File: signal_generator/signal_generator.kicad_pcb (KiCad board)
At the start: 2 copper layers, 100 x 100 mm, 21 parts, among them J1 DAC_OUT, U1 Digilent_CMOD-S7_25, U2 ADC9765, U3 TL072

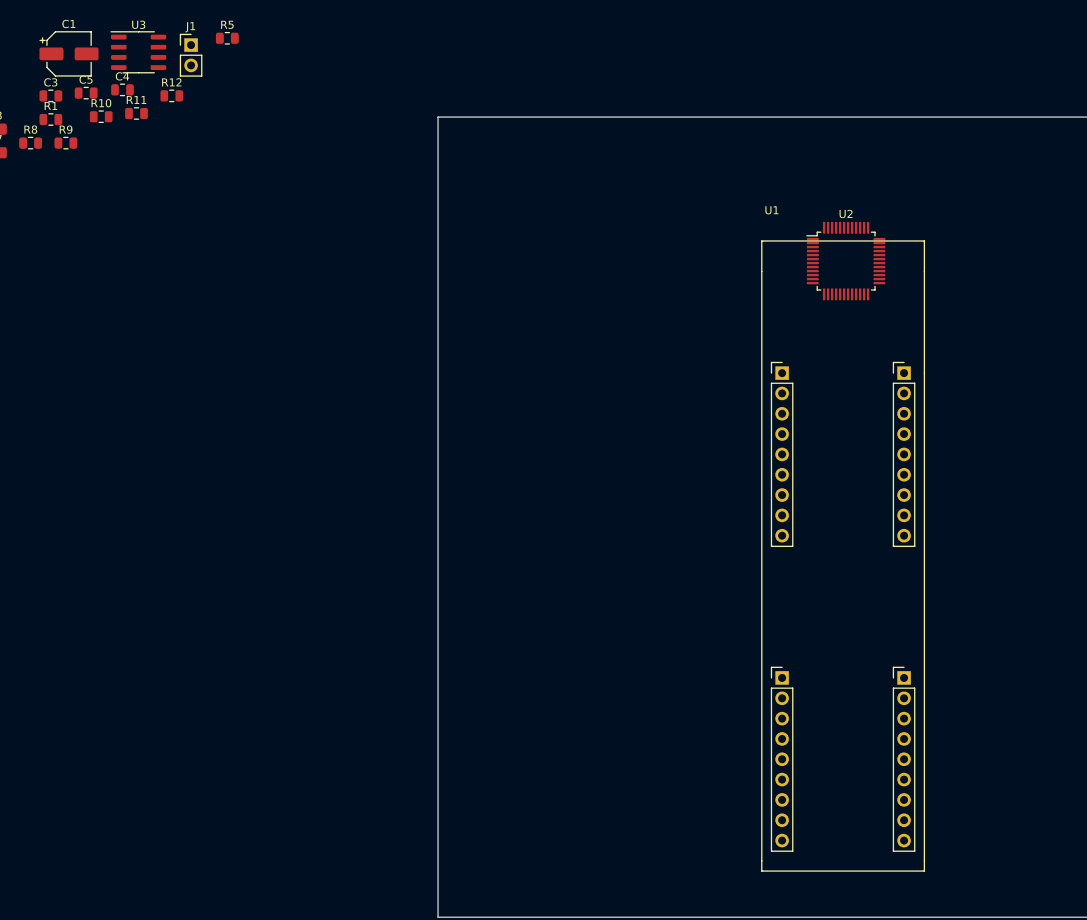
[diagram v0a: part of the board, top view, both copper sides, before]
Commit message: new pcb design and pin layout
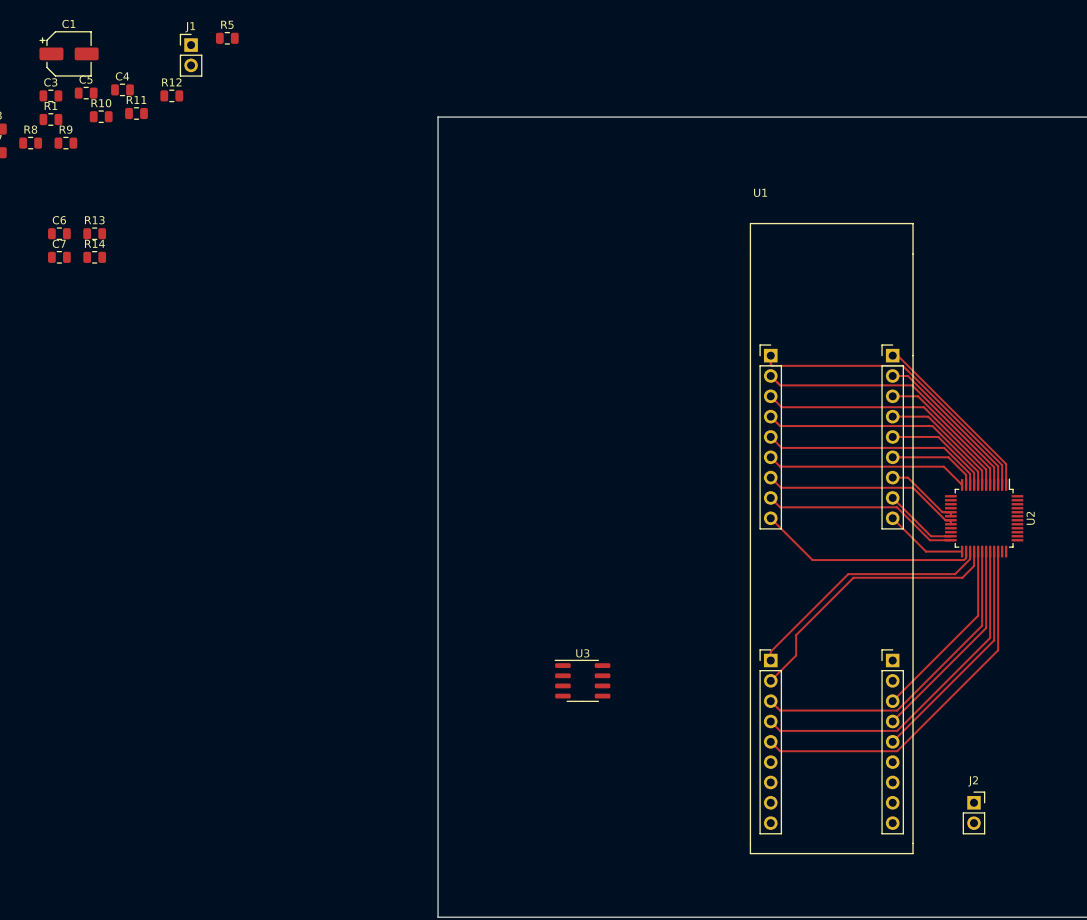
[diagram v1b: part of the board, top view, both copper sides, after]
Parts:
- added C6: 22nF, Capacitor_SMD:C_0805_2012Metric, F.Cu at (106.7, 68.6)
- added C7: 22nF, Capacitor_SMD:C_0805_2012Metric, F.Cu at (106.7, 71.5)
- added J2: USB/Ext., Connector_PinSocket_2.54mm:PinSocket_1x02_P2.54mm_Vertical, F.Cu at (221.0, 139.7)
- added R13: 256, Resistor_SMD:R_0805_2012Metric, F.Cu at (111.1, 68.6)
- added R14: 256, Resistor_SMD:R_0805_2012Metric, F.Cu at (111.1, 71.5)
- moved U3 96.2 mm to (172.1, 124.5)
- moved U2 36.5 mm to (222.2, 104.1), turned to 270 degrees
- moved U1 2.60 mm to (195.6, 83.8)
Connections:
- U1 pad 1: /DB0P1 -> /DB10P1
- U1 pad 16: /DB9P1 -> /DB7P2
- U1 pad 17: /DB10P1 -> /DB6P2
- U1 pad 18: /DB11P1 -> /DB4P2
- U1 pad 19: /DB0P2 -> /DB2P2
- U1 pad 2: /DB1P1 -> /DB8P1
- U1 pad 20: /DB1P2 -> /DB0P2
- U1 pad 21: /BD2P2 -> Net-(U1-Pad21)
- U1 pad 22: /BD3P2 -> Net-(U1-Pad22)
- U1 pad 23: /BD4P2 -> Net-(U1-Pad23)
- U1 pad 24: +5VD -> Net-(J2-Pad2)
- U1 pad 29: Net-(U1-Pad29) -> /DB1P2
- U1 pad 3: /DB2P1 -> /DB6P1
- U1 pad 30: Net-(U1-Pad30) -> /DB3P2
- U1 pad 31: Net-(U1-Pad31) -> /DB5P2
- U1 pad 4: /DB3P1 -> /DB4P1
- U1 pad 40: /SLEEP -> /DB9P2
- U1 pad 41: /CLK_1MHz -> /DB11P2
- U1 pad 42: /BD11P2 -> /CLK_1MHz
- U1 pad 43: /BD10P2 -> /DB1P1
- U1 pad 44: /BD9P2 -> /DB3P1
- U1 pad 45: /BD8P2 -> /DB5P1
- U1 pad 46: /BD7P2 -> /DB7P1
- U1 pad 47: /BD6P2 -> /DB9P1
- U1 pad 48: /BD5P2 -> /DB11P1
- U1 pad 5: /DB4P1 -> /DB2P1
- U1 pad 6: /DB5P1 -> /DB0P1
- U1 pad 7: /DB6P1 -> /CLK_1MHz
- U1 pad 8: /DB7P1 -> /DB10P2
- U1 pad 9: /DB8P1 -> /DB8P2
- U2 pad 16: +5VD -> +3V3
- U2 pad 22: +5VD -> +3V3
- U2 pad 23: /BD11P2 -> /DB11P2
- U2 pad 24: /BD10P2 -> /DB10P2
- U2 pad 25: /BD9P2 -> /DB9P2
- U2 pad 26: /BD8P2 -> /DB8P2
- U2 pad 27: /BD7P2 -> /DB7P2
- U2 pad 28: /BD6P2 -> /DB6P2
- U2 pad 29: /BD5P2 -> /DB5P2
- U2 pad 30: /BD4P2 -> /DB4P2
- U2 pad 31: /BD3P2 -> /DB3P2
- U2 pad 32: /BD2P2 -> /DB2P2
- U2 pad 47: +5VA -> +3.3VA
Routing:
- net /DB0P2: track 0.00 -> 46.5 mm
- net /DB2P2: track 0.00 -> 43.5 mm
- net /DB4P2: track 0.00 -> 40.6 mm
- net /DB10P1: track 0.00 -> 37.7 mm
- net /DB8P1: track 0.00 -> 34.9 mm
- net /CLK_1MHz: track 0.00 -> 34.8 mm
- net /DB6P2: track 0.00 -> 34.7 mm
- net /DB6P1: track 0.00 -> 32.6 mm
- net /DB7P2: track 0.00 -> 31.8 mm
- net /DB4P1: track 0.00 -> 30.4 mm
- net /DB1P2: track 0.00 -> 29.0 mm
- net /DB2P1: track 0.00 -> 28.2 mm
- net /DB8P2: track 0.00 -> 27.5 mm
- net /DB3P2: track 0.00 -> 26.1 mm
- net /DB0P1: track 0.00 -> 25.4 mm
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
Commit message: added power supply, integrated in schematic
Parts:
- removed C4, C5: C_Small, Capacitor_SMD:C_0805_2012Metric
- removed C6, C7: 22nF, Capacitor_SMD:C_0805_2012Metric
- removed J2: USB/Ext., Connector_PinSocket_2.54mm:PinSocket_1x02_P2.54mm_Vertical
- removed R1, R2: 2k, Resistor_SMD:R_0805_2012Metric
- removed R13, R14: 256, Resistor_SMD:R_0805_2012Metric
- removed R3, R4, R5, R6: 25R, Resistor_SMD:R_0805_2012Metric
- removed R9: 225R, Resistor_SMD:R_0805_2012Metric
- removed U1: Digilent_CMOD-S7_25, signal_generator:CMODS7-25
- removed U2: ADC9765, Package_QFP:LQFP-48_7x7mm_P0.5mm
- removed U3: TL072, Package_SO:SOIC-8_3.9x4.9mm_P1.27mm
- added C101: 22nF, Capacitor_SMD:C_0603_1608Metric, F.Cu at (238.5, 100.6)
- added C102: 22nF, Capacitor_SMD:C_0603_1608Metric, F.Cu at (238.5, 90.3)
- added C201: 10u, DSC-Supply:153CLV-0405, F.Cu at (217.4, 129.0)
- added C202: 22u, DSC-Supply:C0805, F.Cu at (231.6, 120.9)
- added C203: 100nF, Capacitor_SMD:C_0603_1608Metric, F.Cu at (232.9, 89.7)
- added C204: 100nF, Capacitor_SMD:C_0603_1608Metric, F.Cu at (249.4, 108.0)
- added C205: 100nF, Capacitor_SMD:C_0603_1608Metric, F.Cu at (219.7, 93.7)
- added C206: 10u, DSC-Supply:153CLV-0405, F.Cu at (221.5, 122.9)
- added C207: 100nF, Capacitor_SMD:C_0603_1608Metric, F.Cu at (219.7, 96.8)
- added C208: 100nF, Capacitor_SMD:C_0603_1608Metric, F.Cu at (237.5, 108.0)
- added C209: 2u2, DSC-Supply:C0805, F.Cu at (227.1, 126.0)
- added C210: 1n, DSC-Supply:C0805, F.Cu at (231.6, 132.1)
- added C211: 22u, DSC-Supply:C0805, F.Cu at (227.1, 132.1)
- added C212: 10u, DSC-Supply:153CLV-0405, F.Cu at (236.7, 127.0)
- added C213: 10u, DSC-Supply:153CLV-0405, F.Cu at (244.9, 127.5)
- added D201: MBR0520LT, DSC-Supply:SOD123, F.Cu at (226.6, 134.6)
- added J101: DAC_OUT_BUF, Connector_PinHeader_2.54mm:PinHeader_1x02_P2.54mm_Vertical, F.Cu at (328.2, 66.9)
- added J201: Power Input, Connector_PinSocket_2.54mm:PinSocket_1x02_P2.54mm_Vertical, F.Cu at (216.9, 134.6)
- added J202: Power Output, Connector_PinHeader_2.54mm:PinHeader_1x05_P2.54mm_Vertical, F.Cu at (230.6, 117.1)
- added L201: 22u, DSC-Supply:L0315, F.Cu at (227.1, 122.9)
- added L202: 22u, DSC-Supply:L0315, F.Cu at (227.1, 129.0)
- added L203: 5uH, Inductor_SMD:L_0805_2012Metric, F.Cu at (234.2, 113.3)
- added R101: 256, Resistor_SMD:R_0603_1608Metric, F.Cu at (238.5, 98.7)
- added R102: 256, Resistor_SMD:R_0603_1608Metric, F.Cu at (238.5, 92.2)
- added R103: 2k, Resistor_SMD:R_0603_1608Metric, F.Cu at (238.5, 96.8)
- added R104: 2k, Resistor_SMD:R_0603_1608Metric, F.Cu at (238.5, 94.1)
- added R105: 25R, Resistor_SMD:R_0603_1608Metric, F.Cu at (234.9, 94.2)
- added R106: 25R, Resistor_SMD:R_0603_1608Metric, F.Cu at (234.9, 97.0)
- added R107: 25R, Resistor_SMD:R_0603_1608Metric, F.Cu at (234.9, 92.2)
- added R108: 25R, Resistor_SMD:R_0603_1608Metric, F.Cu at (234.9, 99.1)
- added R111: 225R, Resistor_SMD:R_0603_1608Metric, F.Cu at (328.2, 115.3)
- added R113: R_Small, Resistor_SMD:R_0603_1608Metric, F.Cu at (337.1, 69.0)
- added R114: R_Small, Resistor_SMD:R_0603_1608Metric, F.Cu at (332.7, 71.9)
- added R117: R_Small, Resistor_SMD:R_0603_1608Metric, F.Cu at (328.1, 74.9)
- added R118: R_Small, Resistor_SMD:R_0603_1608Metric, F.Cu at (332.5, 74.9)
- added R201: 29k4, DSC-Supply:C0805, F.Cu at (231.6, 129.5)
- added R202: 10k, DSC-Supply:C0805, F.Cu at (231.6, 134.6)
- added R203: 30k, DSC-Supply:C0805, F.Cu at (240.8, 123.4)
- added R204: 30k, DSC-Supply:C0805, F.Cu at (240.8, 120.9)
- added R205: 30k, DSC-Supply:C0805, F.Cu at (249.4, 123.4)
- added R206: 30k, DSC-Supply:C0805, F.Cu at (249.4, 120.9)
- added RV101: 10kB, Potentiometer_THT:Potentiometer_Alpha_RD901F-40-00D_Single_Vertical_CircularHoles, F.Cu at (225.1, 59.4)
- added RV102: 10kB, Potentiometer_THT:Potentiometer_Alpha_RD901F-40-00D_Single_Vertical_CircularHoles, F.Cu at (225.1, 73.7)
- added RV103: 10kB, Potentiometer_THT:Potentiometer_Alpha_RD901F-40-00D_Single_Vertical_CircularHoles, F.Cu at (239.9, 59.4)
- added RV104: 10kB, Potentiometer_THT:Potentiometer_Alpha_RD901F-40-00D_Single_Vertical_CircularHoles, F.Cu at (239.9, 73.7)
- added U101: Digilent_CMOD-S7_25, signal_generator:CMODS7-25, F.Cu at (195.1, 72.6)
- added U102: ADC9765, Package_QFP:LQFP-48_7x7mm_P0.5mm, F.Cu at (227.1, 95.0)
- added U103: TL074, Package_SO:SSOP-14_5.3x6.2mm_P0.65mm, F.Cu at (243.6, 108.7)
- added U201: TPS76933, DSC-Supply:SOT23-DBV, F.Cu at (222.0, 127.5)
- added U202: LM2611, DSC-Supply:SOT23-DBV, F.Cu at (231.6, 126.0)
- added U203: TPS76901, DSC-Supply:SOT23-DBV, F.Cu at (240.8, 127.5)
- added U204: TPS72301, DSC-Supply:SOT23-DBV, F.Cu at (249.4, 127.5)
- C103: renamed from C1; footprint Capacitor_SMD:CP_Elec_5x5.3 -> DSC-Supply:153CLV-0405
- C104: renamed from C2; footprint Capacitor_SMD:C_0805_2012Metric -> Capacitor_SMD:C_0603_1608Metric
- C105: renamed from C3; footprint Capacitor_SMD:C_0805_2012Metric -> Capacitor_SMD:C_0603_1608Metric
- R109: renamed from R7; footprint Resistor_SMD:R_0805_2012Metric -> Resistor_SMD:R_0603_1608Metric
- R110: renamed from R8; footprint Resistor_SMD:R_0805_2012Metric -> Resistor_SMD:R_0603_1608Metric
- R112: renamed from R10; footprint Resistor_SMD:R_0805_2012Metric -> Resistor_SMD:R_0603_1608Metric
- R115: renamed from R11; footprint Resistor_SMD:R_0805_2012Metric -> Resistor_SMD:R_0603_1608Metric
- R116: renamed from R12; footprint Resistor_SMD:R_0805_2012Metric -> Resistor_SMD:R_0603_1608Metric
- moved C104 253.5 mm to (324.6, 112.3), turned to 270 degrees
- moved R115 220.4 mm to (329.7, 108.7), turned to 180 degrees
- moved R110 185.1 mm to (278.3, 116.9)
- moved R112 185.1 mm to (287.2, 113.6)
- moved C105 185.1 mm to (280.9, 111.0)
- moved J102 185.1 mm to (298.4, 104.7)
- moved R109 185.1 mm to (273.9, 118.1)
- moved R116 185.1 mm to (296.0, 111.0)
- moved C103 144.0 mm to (242.8, 96.5), turned to 90 degrees
- renumbered J1 to J102
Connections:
- net Net-(C2-Pad1) renamed /I_OUT1-
- net Net-(C2-Pad2) renamed /I_OUT1+
- net Net-(C3-Pad1) renamed /I_OUT2-
- C105 pad 2: Net-(C3-Pad2) -> /I_OUT2+
- J102 pad 2: /DAC_OUT1 -> /DAC_OUT2
- R116 pad 1: /DAC_OUT1 -> /DAC_OUT2
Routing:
- net +3V3: track 0.00 -> 60.0 mm, vias 0 -> 1
- net VDDA: track 0.00 -> 47.5 mm, vias 0 -> 1
- net -5V: track 0.00 -> 38.1 mm
- net /CLK_1MHz: track 34.8 -> 0.00 mm
- net /SLEEP: track 0.00 -> 34.5 mm
- net /CLK_2: track 0.00 -> 31.4 mm
- net +5V: track 0.00 -> 23.5 mm, vias 0 -> 3
- net VSSA: track 0.00 -> 18.3 mm
- net /CLK_1: track 0.00 -> 15.9 mm
- net /I_OUT1-: track 0.00 -> 13.7 mm
- net Net-(C209-Pad2): track 0.00 -> 12.3 mm
- net Net-(C103-Pad1): track 0.00 -> 12.2 mm
- net /I_OUT1+: track 0.00 -> 12.0 mm
- net Net-(C209-Pad1): track 0.00 -> 9.84 mm
- net Net-(R102-Pad1): track 0.00 -> 9.75 mm
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- added copper zone on B.Cu, net +5V
- added copper zone on F.Cu, net GND
- added copper zone on F.Cu, net GNDA
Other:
- board size 100 x 100 mm -> 100 x 85 mm

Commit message: finished PCB v1
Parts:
- added G***: LOGO, resona_logo:Logo_kicad_teeny, F.Cu at (220.0, 68.3)
- C101, C102, C104, C105, C203, C204, C205, C207, C208: footprint Capacitor_SMD:C_0603_1608Metric -> Capacitor_SMD:C_0603_1608Metric_Pad1.08x0.95mm_HandSolder
- C103: footprint DSC-Supply:153CLV-0405 -> Capacitor_SMD:C_0603_1608Metric_Pad1.08x0.95mm_HandSolder
- L203: footprint Inductor_SMD:L_0805_2012Metric -> Inductor_THT:L_Axial_L7.0mm_D3.3mm_P10.16mm_Horizontal_Fastron_MICC
- R101, R102, R103, R104, R105, R106, R107, R108, R109, R110, R111, R112, R113, R114, R115, R116, R117, R118: footprint Resistor_SMD:R_0603_1608Metric -> Resistor_SMD:R_0603_1608Metric_Pad0.98x0.95mm_HandSolder
- RV103, RV104: value 10kB -> 10kA
- U103: footprint Package_SO:SSOP-14_5.3x6.2mm_P0.65mm -> Package_SO:SOIC-14_3.9x8.7mm_P1.27mm
- moved R113 90.2 mm to (254.5, 105.2), turned to 270 degrees
- moved R111 86.5 mm to (242.3, 104.9)
- moved R115 86.0 mm to (244.2, 99.2), turned to 270 degrees
- moved C104 84.5 mm to (241.5, 96.6), turned to 0 degrees
- moved R114 82.8 mm to (254.5, 99.1), turned to 90 degrees
- moved R118 82.1 mm to (253.2, 96.0)
- moved R117 81.7 mm to (253.5, 108.2)
- moved J101 75.6 mm to (256.5, 90.9), turned to 180 degrees
- moved R116 52.1 mm to (244.2, 104.9), turned to 90 degrees
- moved J102 49.7 mm to (251.5, 88.4)
- moved R112 47.6 mm to (240.4, 104.9), turned to 270 degrees
- moved R110 41.9 mm to (240.4, 99.2), turned to 90 degrees
- moved C105 39.4 mm to (241.7, 107.4)
- moved RV101 37.7 mm to (257.0, 79.2), turned to 180 degrees
- moved R109 36.9 mm to (242.3, 99.2), turned to 90 degrees
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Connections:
- C204 pad 2: -5VA -> VSSA
- RV101 pad 1: +3.3VA -> +3V3
- RV102 pad 1: +3.3VA -> +3V3
- U101 pad 21: Net-(U101-Pad21) -> /NC
- U101 pad 22: Net-(U101-Pad22) -> /NC
- U101 pad 23: Net-(U101-Pad23) -> /NC
- U101 pad 24: Net-(U101-Pad24) -> +5V
- U101 pad 26: Net-(U101-Pad26) -> /NC
- U101 pad 27: Net-(U101-Pad27) -> /NC
- U103 pad 11: -5VA -> VSSA
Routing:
- net Net-(RV101-Pad2): track 0.00 -> 69.2 mm
- net /DAC_OUT2: track 0.00 -> 59.5 mm, vias 0 -> 1
- net Net-(RV102-Pad2): track 0.00 -> 57.3 mm, vias 0 -> 1
- net Net-(RV104-Pad2): track 0.00 -> 49.6 mm
- net Net-(RV103-Pad2): track 0.00 -> 44.1 mm, vias 0 -> 2
- net +3V3: track 60.0 -> 103.6 mm
- net /DAC_OUT1: track 0.00 -> 42.5 mm
- net +5V: track 23.5 -> 47.7 mm
- net VSSA: track 18.3 -> 42.4 mm, vias 0 -> 1
- net VDDA: track 47.5 -> 69.4 mm, vias 1 -> 2
- net /DAC_OUT1_BUF: track 0.00 -> 21.4 mm
- net /I_OUT2+: track 4.16 -> 19.5 mm
- net /I_OUT2-: track 3.25 -> 17.5 mm
- net GNDA: track 0.95 -> 13.9 mm, vias 0 -> 35
- net /DAC_OUT2_BUF: track 0.00 -> 11.8 mm
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- added copper zone on B.Cu, net GND
- added copper zone on B.Cu, net GNDA
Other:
- board size 100 x 85 mm -> 71 x 85 mm
- rule pad_to_mask_clearance: 0.051 -> 0
- board text added: "Amplitude"
- board text added: "Buffered Output"
- board text added: "CH 1"
- board text added: "CH 2"
- board text added: "CMOD S7 2CH Analog Output Shield"
- board text added: "Frequency"
- board text added: "JLCJLCJLCJLC"
- board text added: "Unbuffered Output"

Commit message: added author to pcb
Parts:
- moved J102 2.54 mm to (251.5, 90.9), turned to 180 degrees
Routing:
- net /DAC_OUT2: track 59.5 -> 57.8 mm, vias 1 -> 0
- net +5V: track 47.7 -> 49.4 mm, vias 3 -> 2
- net /DAC_OUT1: track 42.5 -> 41.2 mm
- net GNDA: vias 35 -> 34
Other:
- board text added: "+3,3"
- board text added: "+4V"
- board text added: "-4V"
- board text added: "CH1"
- board text added: "CH2"
- board text added: "GND"
- board text added: "GNDA"
- board text added: "Lukas Güldenstein Resona Audio 11/2020"

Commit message: send to production
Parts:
- moved R118 3.31 mm to (254.5, 99.1), turned to 270 degrees
- moved R117 2.97 mm to (254.5, 105.4), turned to 90 degrees
- moved R113 2.05 mm to (256.5, 105.4)
- moved R114 2.03 mm to (256.5, 99.1)
- moved G*** 1.70 mm to (219.2, 66.8)
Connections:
- R113 pad 2: Net-(R113-Pad2) -> GNDA
- R114 pad 2: Net-(R114-Pad2) -> GNDA
- R117 pad 2: Net-(R113-Pad2) -> Net-(R113-Pad1)
- R118 pad 2: Net-(R114-Pad2) -> Net-(R114-Pad1)
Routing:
- net Net-(R114-Pad2): track 2.47 -> 0.00 mm
- net Net-(R113-Pad2): track 2.36 -> 0.00 mm
- net Net-(R114-Pad1): track 2.72 -> 4.80 mm
- net Net-(R113-Pad1): track 2.73 -> 4.70 mm
- net GND: track 16.9 -> 18.4 mm
- net /DAC_OUT2_BUF: track 11.8 -> 13.3 mm
- net /DAC_OUT1_BUF: track 21.4 -> 21.1 mm, vias 0 -> 1
- net GNDA: vias 34 -> 35
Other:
- board size 71 x 85 mm -> 69.3 x 83.3 mm

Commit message: final status
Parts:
- removed G***: LOGO, resona_logo:Logo_kicad_teeny
- R101, R102: value 256 -> 240R
- R105, R106, R107, R108: value 25R -> 27R
- R109, R110, R111, R112: value 225R -> 2k2
- R113, R114, R117, R118: value R_Small -> 10k
- R115, R116: value 500R -> 4k7
- R203: value 30k -> 360k
- R204: value 30k -> 150k
- R205: value 30k -> 68k
- R206: value 30k -> 27k
- U103: value TL074 -> TL074/TLV3544
